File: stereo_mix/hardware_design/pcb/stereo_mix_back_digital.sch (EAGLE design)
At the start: 194 parts, among them IC1 4051D, IC2 AMS1117-3.3, J1 WQP-PJ301M-12_JACK, J10 WQP-PJ301M-12_JACK, J11 WQP-PJ301M-12_JACK, J12 WQP-PJ301M-12_JACK, J13 WQP-PJ301M-12_JACK, J14 WQP-PJ301M-12_JACK, J15 WQP-PJ301M-12_JACK, J16 WQP-PJ301M-12_JACK, J17 CORTEX_DEBUG_PTH, J18 WQP-PJ301M-12_JACK, J19 WQP-PJ301M-12_JACK, J2 WQP-PJ301M-12_JACK, J3 WQP-PJ301M-12_JACK, J4 WQP-PJ301M-12_JACK, J5 WQP-PJ301M-12_JACK, J6 WQP-PJ301M-12_JACK, J7 WQP-PJ301M-12_JACK, J8 WQP-PJ301M-12_JACK, J9 WQP-PJ301M-12_JACK, U1 MCP4822E-SN, U10 MCP4822E-SN, U11 MCP6002T-I/SN, U12 MCP6002T-I/SN, U13 MCP4922E/SL, U14 MCP4922E/SL, U15 TL072CD, U16 TL072CD, U17 MCP6002T-I/SN, U18 MCP6002T-I/SN, U19 MCP6002T-I/SN, U2 MCP4822E-SN, U20 MCP6002T-I/SN, U21 STM32F030C8T6, U22 TL072CD, U3 MCP6002T-I/SN, U4 MCP6002T-I/SN, U5 MCP4922E/SL, U6 MCP4922E/SL, U7 TL072CD, U8 TL072CD, U9 MCP4822E-SN, X1 8MHz

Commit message: stereo mix routing nearly finished
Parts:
- added C43, C44, C45, C46, C57, C58, C59, C60, C61, C62, C63, C64: 100nF, jhbruhn-cr:C-EUC0402
- added C47, C48: 22uF, jhbruhn-cdr:C-EUC0805
- added C49, C50, C51, C52, C53, C54, C55, C56: 10uF, jhbruhn-cr:C-EUC0402
- added R91, R92, R93, R94: 100R, jhbruhn-cdr:R-EU_R0402
- C32, C33: value 6.8pF -> 220pF
- D1, D2: value SS54 -> B5819W; device jhbruhn-cdr:DIODE-SMA -> jhbruhn-cdr:DIODE-SOD123
- IC1: value 4051D -> 4051CD4051; device jhbruhn-ic:4051D -> jhbruhn-ic:4051CD4051
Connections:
- removed net +5V: U13.!SHDN, U13.VDD, U14.!SHDN, U14.VDD, U5.!SHDN, U5.VDD, U6.!SHDN, U6.VDD
- new net LED_1: R91.1, U21.PB7/I2C1_SDA/USART1_RX/TIM17_CH1N
- new net LED_2: R92.1, U21.PB15/SPI2_MOSI/TIM1_CH3N/TIM15_CH1N/TIM15_CH2/RTC_REFIN
- new net LED_3: R93.1, U21.PC13/RTC_TAMP1/RTC_TS/RTC_OUT/WKUP2
- new net LED_4: R94.1, U21.PC14/OSC32_IN
- new net N$12: R91.2, SW1LED.A
- new net N$13: R92.2, SW2LED.A
- new net N$18: R93.2, SW3LED.A
- new net N$42: R94.2, SW4LED.A
- new net SWITCH_1: SW1SWITCH.1, SW1SWITCH.3, U21.PA12/USART1_RTS/TIM1_ETR/EVENTOUT
- new net SWITCH_2: SW2SWITCH.1, SW2SWITCH.3, U21.PB1/TIM3_CH4/TIM14_CH1/TIM1_CH3N/ADC_IN9
- new net SWITCH_3: SW3SWITCH.1, SW3SWITCH.3, U21.PB2
- new net SWITCH_4: SW4SWITCH.1, SW4SWITCH.3, U21.PB6/I2C1_SCL/USART1_TX/TIM16_CH1N
- net +12V: now also C48.1
- net +3V3: now also C43.1, C44.1, C45.1, C46.1, C49.1, C50.1, C51.1, C52.1, C53.1, C54.1, C55.1, C56.1, U13.!SHDN, U13.VDD, U14.!SHDN, U14.VDD, U5.!SHDN, U5.VDD, U6.!SHDN, U6.VDD
- net -12V: now also C47.2
- net 1_IN_L: now also J2.3
- net 2_IN_L: now also J4.3
- net 3_IN_L: now also J6.3
- net 4_IN_L: now also J8.3
- net GND: now also C43.2, C44.2, C45.2, C46.2, C47.1, C48.2, C49.2, C50.2, C51.2, C52.2, C53.2, C54.2, C55.2, C56.2, C57.2, C58.2, C59.2, C60.2, C61.2, C62.2, C63.2, C64.2, SW1LED.C, SW1SWITCH.2, SW1SWITCH.4, SW2LED.C, SW2SWITCH.2, SW2SWITCH.4, SW3LED.C, SW3SWITCH.2, SW3SWITCH.4, SW4LED.C, SW4SWITCH.2, SW4SWITCH.4
- net OUT_L: now also J18.3
- net PAN_1_POT: now also C61.1
- net PAN_2_POT: now also C62.1
- net PAN_3_POT: now also C63.1
- net PAN_4_POT: now also C64.1
- net VOL_1_POT: now also C57.1
- net VOL_2_POT: now also C58.1
- net VOL_3_POT: now also C59.1
- net VOL_4_POT: now also C60.1
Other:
- moved on the sheet: SW1LED, SW1SWITCH, SW2LED, SW2SWITCH, SW3LED, SW3SWITCH, SW4LED, SW4SWITCH

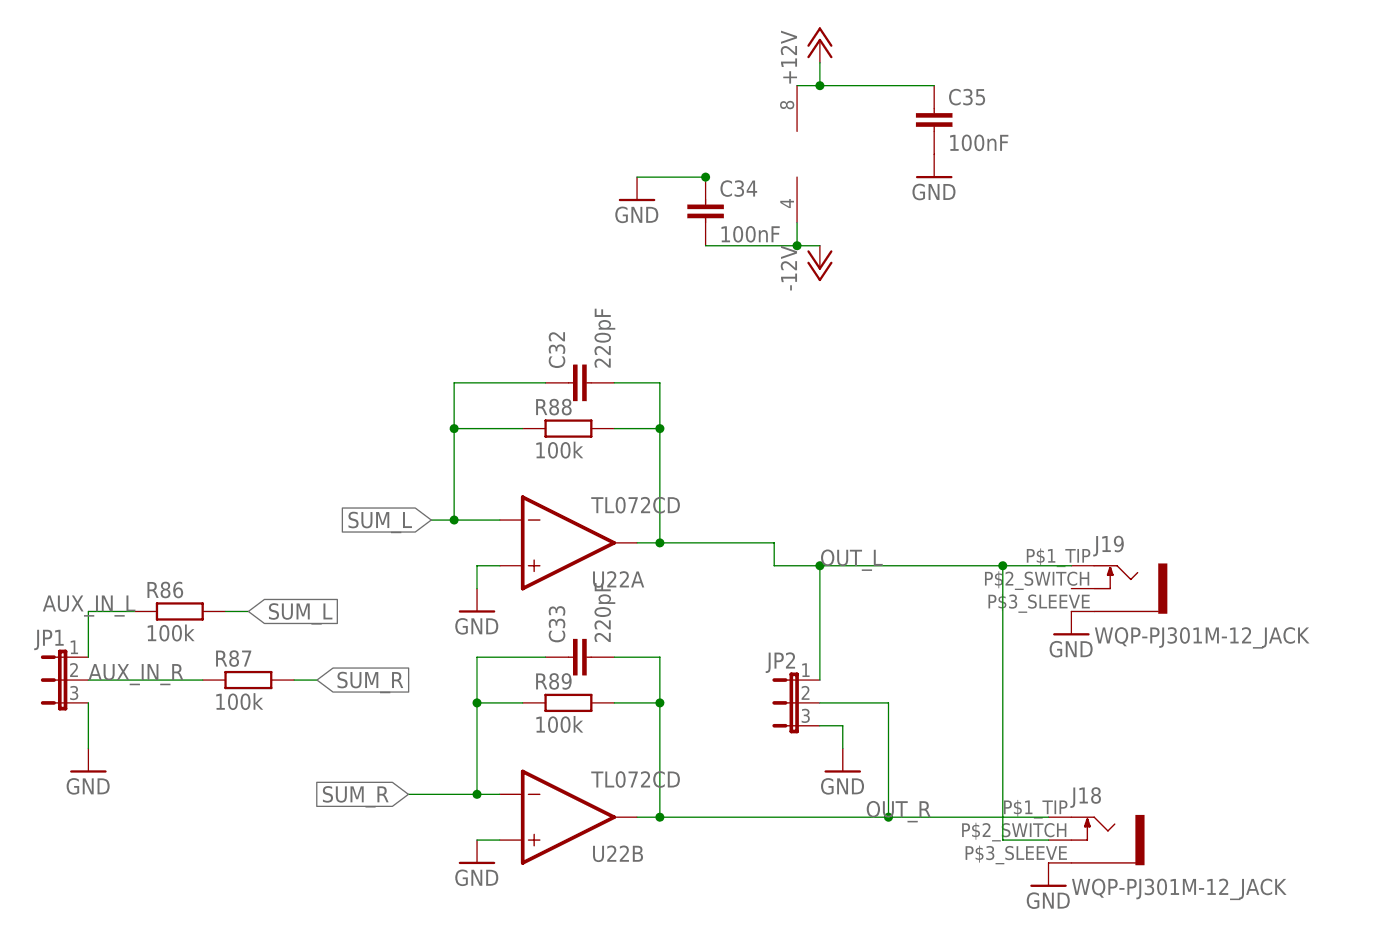
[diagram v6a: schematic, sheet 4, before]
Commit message: All very important signals routed
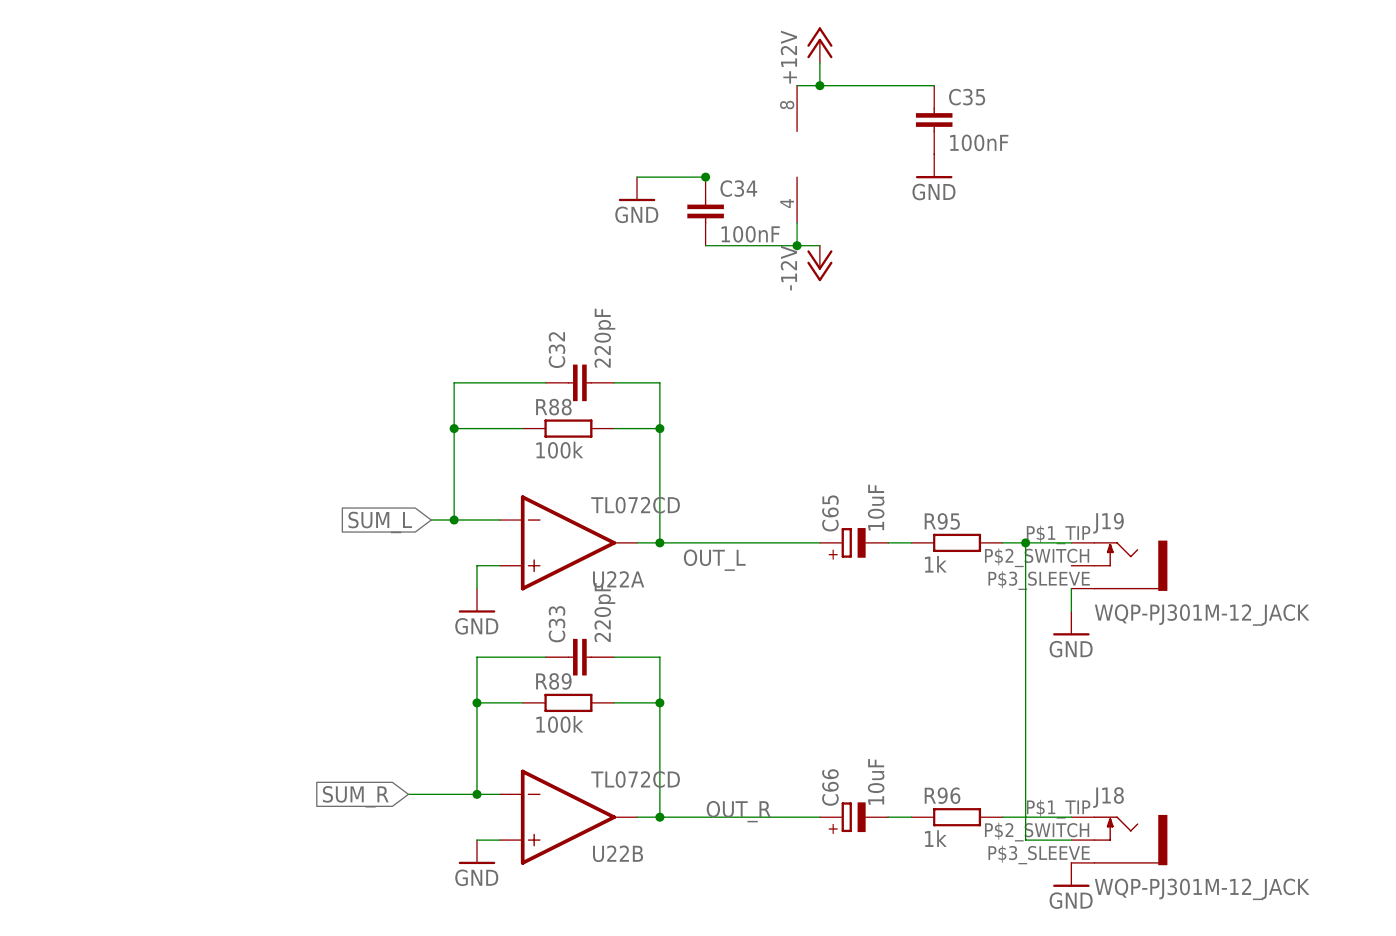
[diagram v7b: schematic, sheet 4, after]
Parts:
- removed JP1, JP2: (no value), jumper:JP2E
- removed R86, R87: 100k, jhbruhn-cr:R-EU_R0402
- added C65, C66: 10uF, jhbruhn-cdr:CPOL-EUA/3216-18R
- added R95, R96: 1k, jhbruhn-cdr:R-EU_R0402
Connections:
- removed net AUX_IN_L: JP1.1, R86.1
- removed net AUX_IN_R: JP1.2, R87.1
- new net N$43: J18.3, J19.2, R95.2
- new net N$45: C65.-, R95.1
- new net N$56: J18.2, R96.2
- new net N$57: C66.-, R96.1
- net GND: no longer JP1.3, JP2.3
- net OUT_L: now also C65.+; no longer J18.3, J19.2, JP2.1
- net OUT_R: now also C66.+; no longer J18.2, JP2.2
- net SUM_L: no longer R86.2
- net SUM_R: no longer R87.2
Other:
- moved on the sheet: J18, J19
